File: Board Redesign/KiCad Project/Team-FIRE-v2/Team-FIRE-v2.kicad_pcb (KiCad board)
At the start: 4 copper layers, 95.3 x 88.9 mm, 88 parts, among them IC1 MCP1826T-3302E_DC, IC2 BTS500601TEAAUMA2, J1 47388-2001, J10 PCB.MMCX.F.ST.SMT.JACK.HT, J2 53885-0408, J3 UX60-MB-5ST, J4 Conn_01x03, J5 Conn_ARM_JTAG_SWD_10, J6 Conn_01x03, J7 Conn_01x03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

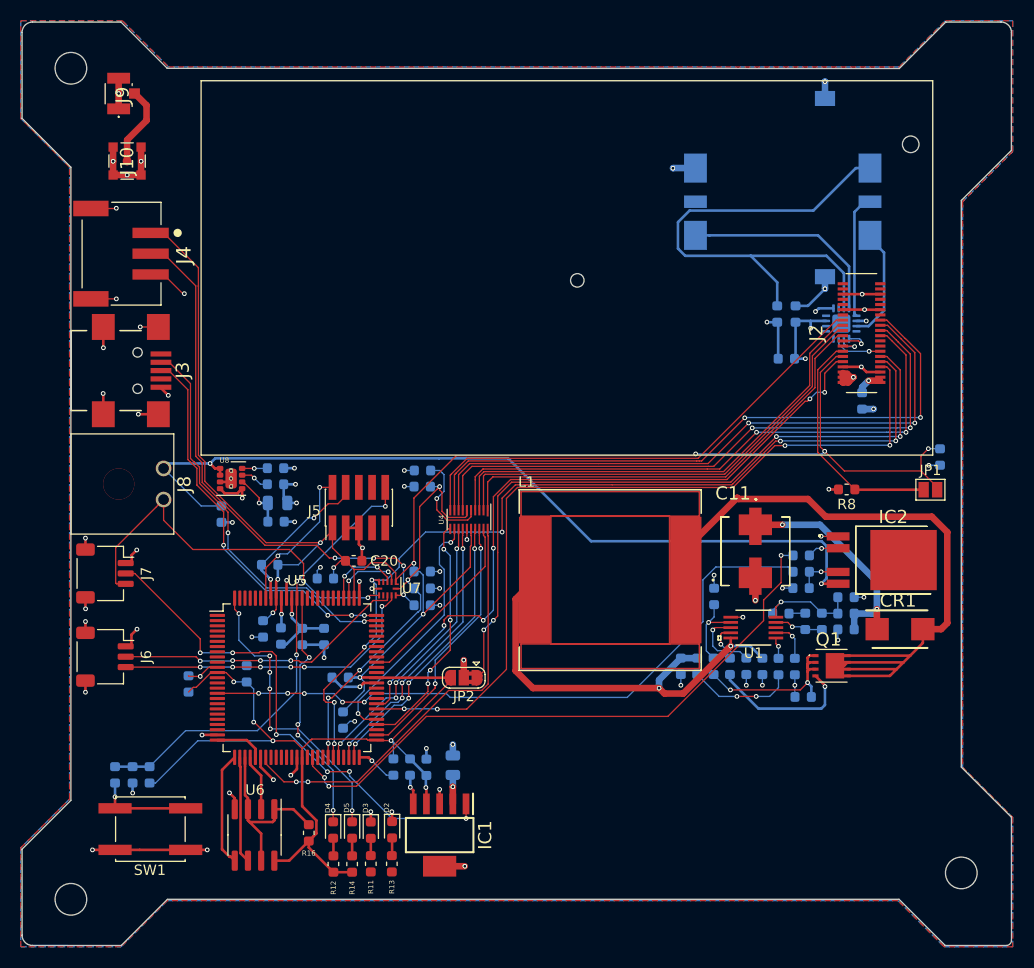
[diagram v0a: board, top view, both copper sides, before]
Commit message: Increased trace width for boost circuitry & added silk screen
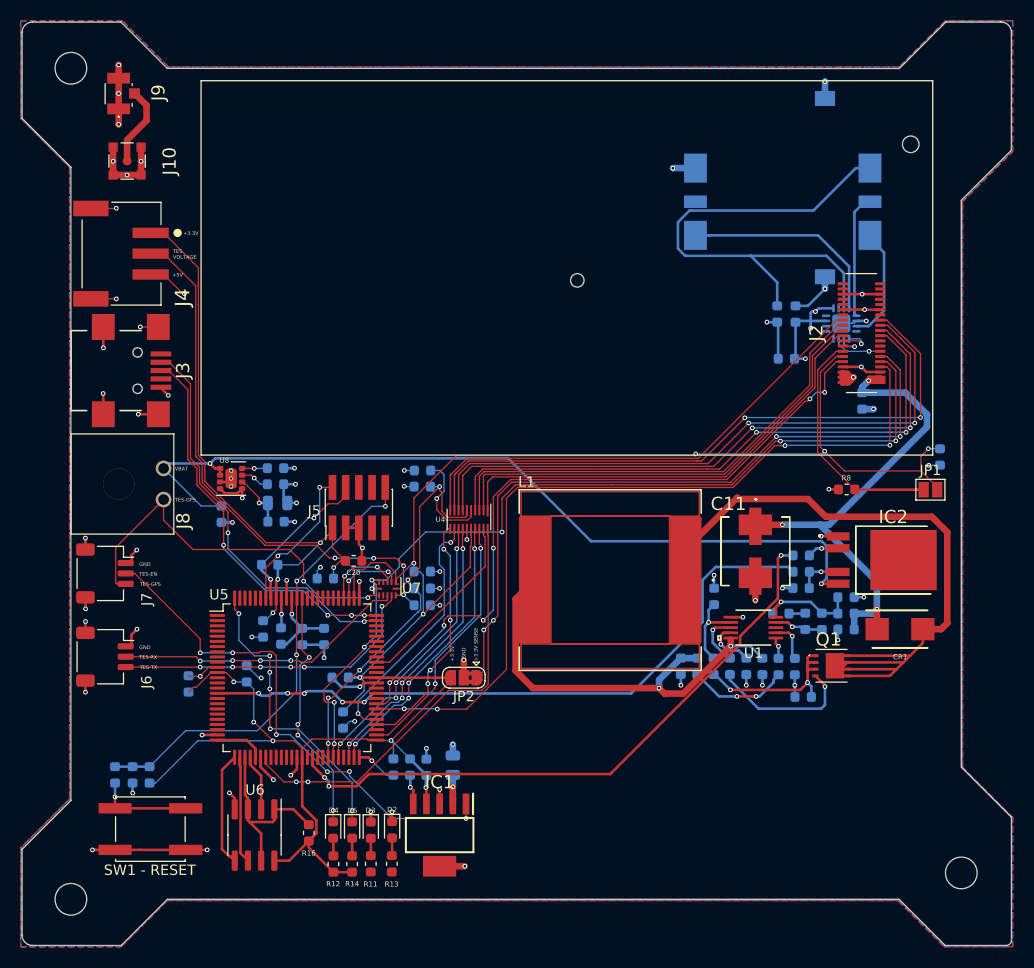
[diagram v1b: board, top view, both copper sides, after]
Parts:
- SW1 - RESET: renamed from SW1
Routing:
- net +30V: track 25.0 -> 52.9 mm
- net GND: track 132.6 -> 140.3 mm, vias 67 -> 70
- net 8V_ISENSE: track 64.0 -> 65.7 mm
- net +5V: track 29.6 -> 30.9 mm
- net Net-(C2-Pad1): track 10.3 -> 9.72 mm
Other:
- board text added: "+3.3V"
- board text added: "+3.3V SENSE"
- board text added: "+5V"
- board text added: "GND"
- board text added: "TES VOLTAGE"
- board text added: "TES-EN"
- board text added: "TES-GPS"
- board text added: "TES-RX"
- board text added: "TES-TX"
- board text added: "VBAT"

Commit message: Deleted unused LED's, finished mounting for IRIDIUM
- Delete the two unused LEDs from schematic and layout
- Added grounding vias for antenna connection
- Added grounding vias for IRIDIUM 9523 modem
- Added keepout zones (except GND) for antenna and modem
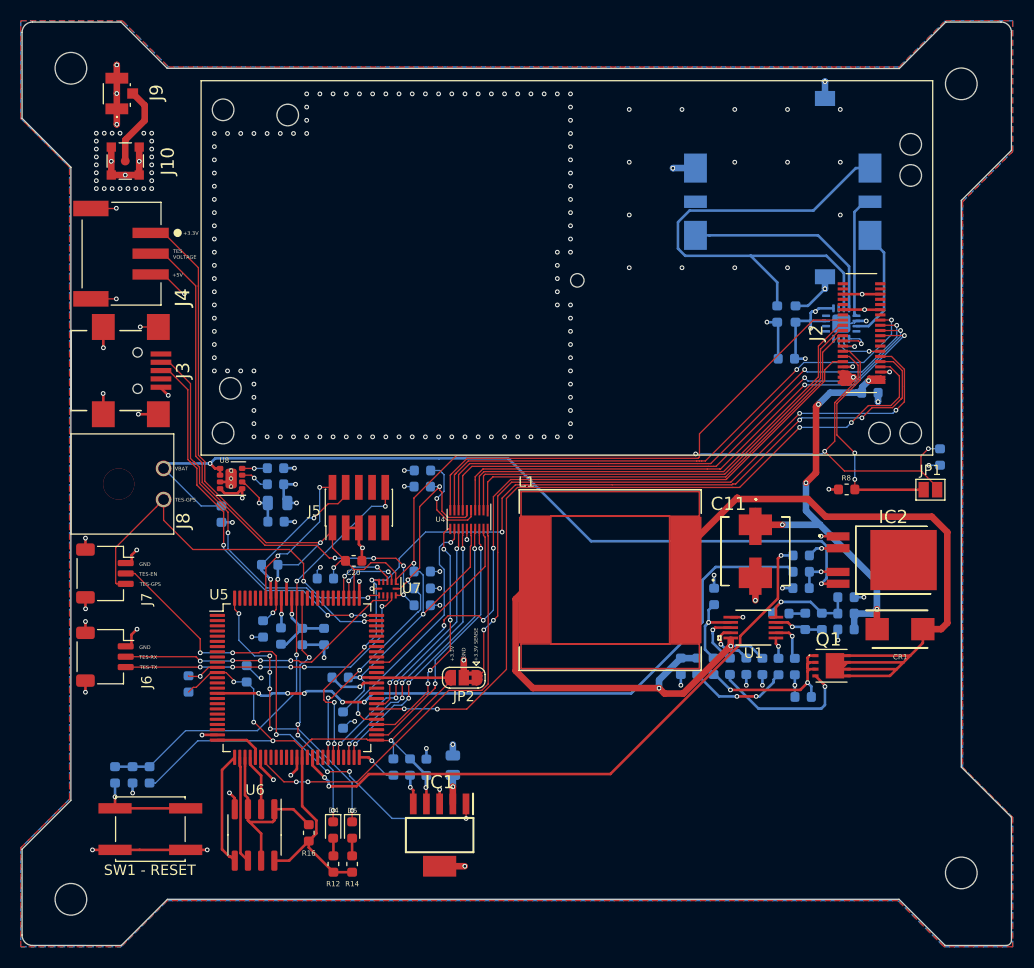
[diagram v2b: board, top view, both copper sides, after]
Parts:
- removed D2: Blue, LED_SMD:LED_0603_1608Metric
- removed D3: Green, LED_SMD:LED_0603_1608Metric
- removed R11, R13: 330, Resistor_SMD:R_0603_1608Metric
- moved C16 1.08 mm to (107.0, 61.1), turned to 0 degrees
- moved J10 0.18 mm to (35.3, 38.8)
- moved J9 0.18 mm to (34.5, 32.3)
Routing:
- net RX: track 62.0 -> 53.6 mm
- net CTS: track 60.6 -> 54.0 mm
- net DSR: track 59.3 -> 53.8 mm
- net +30V: track 52.9 -> 47.7 mm, vias 3 -> 5
- net RTS: track 57.2 -> 52.5 mm
- net GND: track 140.3 -> 136.2 mm, vias 70 -> 218
- net Net-(D2-Pad2): track 1.71 -> 0.00 mm
- net Net-(D3-Pad2): track 1.66 -> 0.00 mm
- net TX: track 47.4 -> 48.7 mm
- net BOOST_EN: track 77.9 -> 76.7 mm
- net 3.3V_SENSE: track 68.3 -> 67.2 mm
- net TX_ACTIVE: track 88.3 -> 87.2 mm
- net MODE_SW: track 261.4 -> 262.3 mm
- net PWR_EN: track 67.9 -> 68.1 mm, vias 6 -> 4
- net RF_EN: track 22.8 -> 22.6 mm, vias 0 -> 2
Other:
- outline, holes or cut-outs redrawn

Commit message: Moved some stuff
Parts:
- moved L1 30.2 mm to (104.3, 99.5)
- turned C21 to 90 degrees
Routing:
- net TX: track 48.7 -> 168.4 mm
- net MODE_SW: track 262.3 -> 297.3 mm, vias 15 -> 17
- net Net-(CR1-Pad2): track 70.3 -> 43.6 mm
- net +30V: track 47.7 -> 68.7 mm
- net +8V: track 42.6 -> 31.8 mm, vias 2 -> 3
- net RX: track 53.6 -> 51.8 mm
- net CTS: track 54.0 -> 52.2 mm
- net DSR: track 53.8 -> 52.1 mm
- net RTS: track 52.5 -> 51.0 mm
- net DCD: track 46.5 -> 45.1 mm
- net RI: track 45.8 -> 44.4 mm
- net DTR: track 44.9 -> 43.9 mm
- net GND: track 136.2 -> 136.4 mm, vias 218 -> 217
